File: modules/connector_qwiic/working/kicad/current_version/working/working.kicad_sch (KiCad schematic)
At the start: 1 part, among them J1 h4psmra

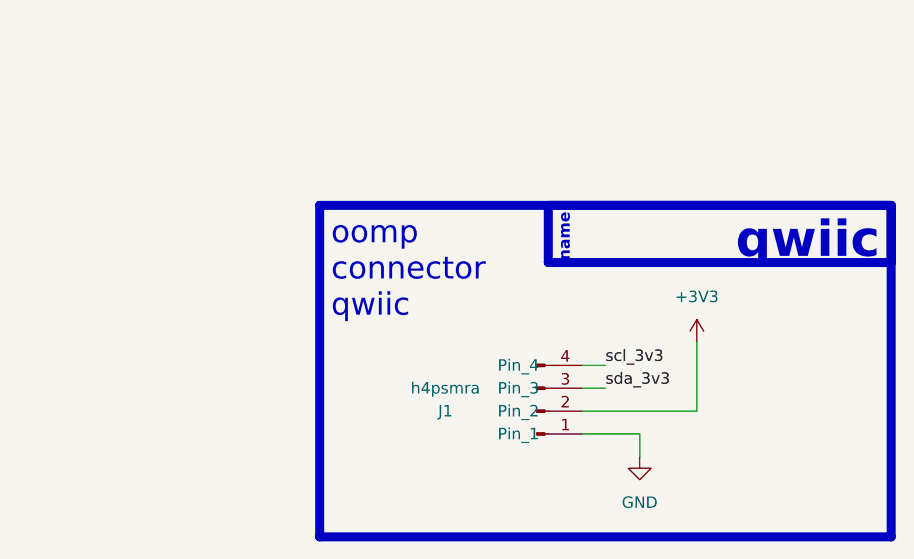
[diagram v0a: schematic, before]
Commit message: fixed formatting to be more consistent
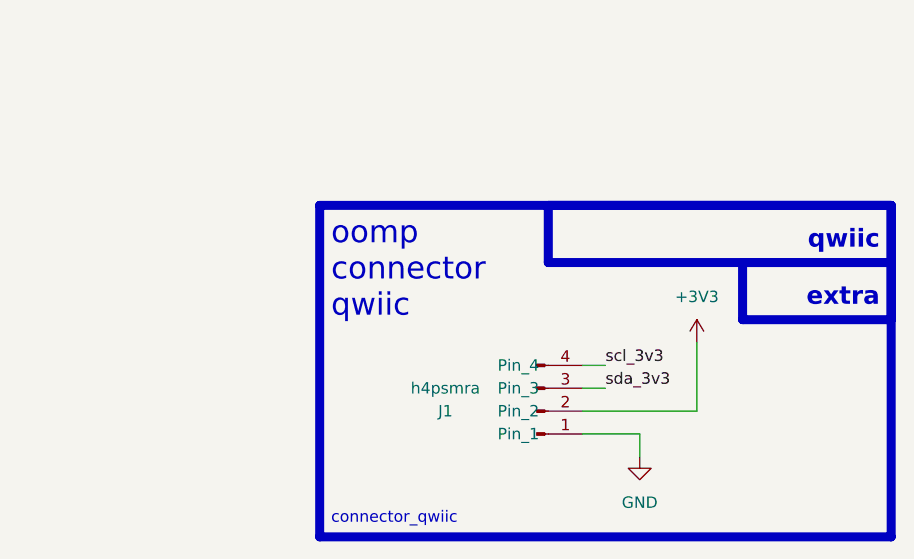
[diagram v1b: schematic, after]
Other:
- note added: "connector_qwiic"
- note added: "extra"
- note removed: "name"
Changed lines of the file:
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@@
   (rectangle (start 132.08 71.12) (end 170.18 77.47)
     (stroke (width 1) (type default))
-    (fill (type color) (color 0 0 0 0))
+    (fill (type none))
   )
-  (text "qwiic\n" (at 168.91 77.47 0)
-    (effects (font (size 4 4) (thickness 0.8) bold (color 255 255 255 1)) (justify right bottom))
+  (rectangle (start 153.67 77.47) (end 170.18 83.82)
+    (stroke (width 1) (type default))
+    (fill (type none))
   )
-  (text "name" (at 134.62 77.47 90)
-    (effects (font (size 1.27 1.27) (thickness 0.254) bold (color 255 255 255 1)) (justify left bottom))
+  (text "qwiic\n" (at 168.91 76.2 0)
+    (effects (font (size 2 2) (thickness 0.8) bold) (justify right bottom))
   )
   (text "oomp\nconnector\nqwiic\n" (at 107.95 83.82 0)
     (effects (font (size 2.5 2.5)) (justify left bottom))
   )
+  (text "extra" (at 168.91 82.55 0)
+    (effects (font (size 2 2) (thickness 0.8) bold) (justify right bottom))
+  )
+  (text "connector_qwiic" (at 107.95 106.68 0)
+    (effects (font (size 1.27 1.27)) (justify left bottom))
+  )
   (label "scl_3v3" (at 138.43 88.9 0) (fields_autoplaced)

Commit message: schematic formatting
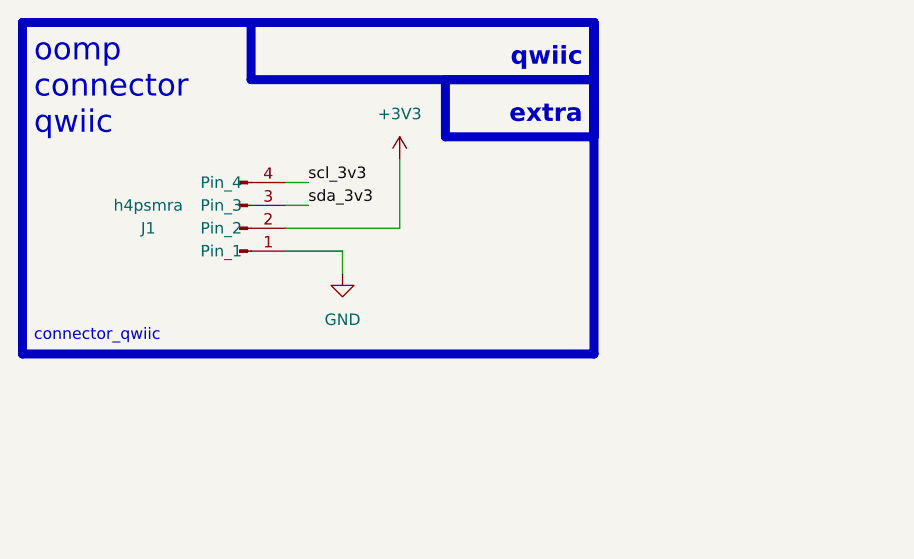
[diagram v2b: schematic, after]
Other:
- moved on the sheet: J1
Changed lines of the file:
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@@
 (kicad_sch (version 20230121) (generator eeschema)
-  (paper "A4")
-  (wire (pts (xy 142.24 96.52) (xy 142.24 99.06))
+  (paper "A5")
+  (wire (pts (xy 109.22 76.2) (xy 109.22 78.74))
     (stroke (width 0) (type default))
   )
-  (wire (pts (xy 135.89 93.98) (xy 148.59 93.98))
+  (wire (pts (xy 102.87 73.66) (xy 115.57 73.66))
     (stroke (width 0) (type default))
   )
-  (wire (pts (xy 142.24 96.52) (xy 135.89 96.52))
+  (wire (pts (xy 109.22 76.2) (xy 102.87 76.2))
     (stroke (width 0) (type default))
   )
-  (wire (pts (xy 135.89 91.44) (xy 138.43 91.44))
+  (wire (pts (xy 102.87 71.12) (xy 105.41 71.12))
     (stroke (width 0) (type default))
   )
-  (wire (pts (xy 135.89 88.9) (xy 138.43 88.9))
+  (wire (pts (xy 102.87 68.58) (xy 105.41 68.58))
     (stroke (width 0) (type default))
   )
-  (wire (pts (xy 148.59 93.98) (xy 148.59 86.36))
+  (wire (pts (xy 115.57 73.66) (xy 115.57 66.04))
     (stroke (width 0) (type default))
   )
-  (rectangle (start 106.68 71.12) (end 170.18 107.95)
+  (rectangle (start 73.66 50.8) (end 137.16 87.63)
     (stroke (width 1) (type default))
     (fill (type none))
   )
-  (rectangle (start 151.13 234.95) (end 151.13 234.95)
+  (rectangle (start 118.11 214.63) (end 118.11 214.63)
     (stroke (width 0) (type default))
     (fill (type none))
   )
-  (rectangle (start 132.08 71.12) (end 170.18 77.47)
+  (rectangle (start 99.06 50.8) (end 137.16 57.15)
     (stroke (width 1) (type default))
     (fill (type none))
   )
-  (rectangle (start 153.67 77.47) (end 170.18 83.82)
+  (rectangle (start 120.65 57.15) (end 137.16 63.5)
     (stroke (width 1) (type default))
     (fill (type none))
   )
-  (text "qwiic\n" (at 168.91 76.2 0)
+  (text "qwiic\n" (at 135.89 55.88 0)
     (effects (font (size 2 2) (thickness 0.8) bold) (justify right bottom))
   )
-  (text "oomp\nconnector\nqwiic\n" (at 107.95 83.82 0)
+  (text "oomp\nconnector\nqwiic\n" (at 74.93 63.5 0)
     (effects (font (size 2.5 2.5)) (justify left bottom))
   )
-  (text "extra" (at 168.91 82.55 0)
+  (text "extra" (at 135.89 62.23 0)
     (effects (font (size 2 2) (thickness 0.8) bold) (justify right bottom))
   )
-  (text "connector_qwiic" (at 107.95 106.68 0)
+  (text "connector_qwiic" (at 74.93 86.36 0)
     (effects (font (size 1.27 1.27)) (justify left bottom))
   )
-  (label "scl_3v3" (at 138.43 88.9 0) (fields_autoplaced)
+  (label "scl_3v3" (at 105.41 68.58 0) (fields_autoplaced)
     (effects (font (size 1.27 1.27)) (justify left bottom))
   )
-  (label "sda_3v3" (at 138.43 91.44 0) (fields_autoplaced)
+  (label "sda_3v3" (at 105.41 71.12 0) (fields_autoplaced)
     (effects (font (size 1.27 1.27)) (justify left bottom))
   )
-  (symbol (lib_id "oomlout_oomp_part_symbols:h4psmra_electronic_header_1_mm_jst_sh_4_pin_surface_mount_right_angle") (at 130.81 93.98 0) (mirror x) (unit 1)
+  (symbol (lib_id "oomlout_oomp_part_symbols:h4psmra_electronic_header_1_mm_jst_sh_4_pin_surface_mount_right_angle") (at 97.79 73.66 0) (mirror x) (unit 1)
     (in_bom yes) (on_board yes) (dnp no)
-    (property "Reference" "J1" (at 120.65 93.98 0)
+    (property "Reference" "J1" (at 87.63 73.66 0)
       (effects (font (size 1.27 1.27)))
     )
-    (property "Value" "h4psmra" (at 120.65 91.44 0)
+    (property "Value" "h4psmra" (at 87.63 71.12 0)
       (effects (font (size 1.27 1.27)))
     )
-    (property "Footprint" "oomlout_oomp_part_footprints:h4psmra_electronic_header_1_mm_jst_sh_4_pin_surface_mount_right_angle" (at 130.81 93.98 0)
+    (property "Footprint" "oomlout_oomp_part_footprints:h4psmra_electronic_header_1_mm_jst_sh_4_pin_surface_mount_right_angle" (at 97.79 73.66 0)
       (effects (font (size 1.27 1.27)) hide)
     )
-    (property "Datasheet" "https://github.com/oomlout/oomlout_oomp_v3/parts/electronic_header_1_mm_jst_sh_4_pin_surface_mount_right_angle/datasheet.pdf" (at 130.81 93.98 0)
+    (property "Datasheet" "https://github.com/oomlout/oomlout_oomp_v3/parts/electronic_header_1_mm_jst_sh_4_pin_surface_mount_right_angle/datasheet.pdf" (at 97.79 73.66 0)
       (effects (font (size 1.27 1.27)) hide)
     )
@@
     )
   )
-  (symbol (lib_id "power:GND") (at 142.24 99.06 0) (unit 1)
+  (symbol (lib_id "power:GND") (at 109.22 78.74 0) (unit 1)
     (in_bom yes) (on_board yes) (dnp no) (fields_autoplaced)
-    (property "Reference" "#PWR01" (at 142.24 105.41 0)
+    (property "Reference" "#PWR01" (at 109.22 85.09 0)
       (effects (font (size 1.27 1.27)) hide)
     )
-    (property "Value" "GND" (at 142.24 104.14 0)
+    (property "Value" "GND" (at 109.22 83.82 0)
       (effects (font (size 1.27 1.27)))
     )
-    (property "Footprint" "" (at 142.24 99.06 0)
+    (property "Footprint" "" (at 109.22 78.74 0)
       (effects (font (size 1.27 1.27)) hide)
     )
-    (property "Datasheet" "" (at 142.24 99.06 0)
+    (property "Datasheet" "" (at 109.22 78.74 0)
       (effects (font (size 1.27 1.27)) hide)
     )
@@
     )
   )
-  (symbol (lib_id "power:+3V3") (at 148.59 86.36 0) (unit 1)
+  (symbol (lib_id "power:+3V3") (at 115.57 66.04 0) (unit 1)
     (in_bom yes) (on_board yes) (dnp no) (fields_autoplaced)
-    (property "Reference" "#PWR02" (at 148.59 90.17 0)
+    (property "Reference" "#PWR02" (at 115.57 69.85 0)
       (effects (font (size 1.27 1.27)) hide)
     )
-    (property "Value" "+3V3" (at 148.59 81.28 0)
+    (property "Value" "+3V3" (at 115.57 60.96 0)
       (effects (font (size 1.27 1.27)))
     )
-    (property "Footprint" "" (at 148.59 86.36 0)
+    (property "Footprint" "" (at 115.57 66.04 0)
       (effects (font (size 1.27 1.27)) hide)
     )
-    (property "Datasheet" "" (at 148.59 86.36 0)
+    (property "Datasheet" "" (at 115.57 66.04 0)
       (effects (font (size 1.27 1.27)) hide)
     )
